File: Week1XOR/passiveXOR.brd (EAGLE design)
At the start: 100 x 80 mm, 27 parts

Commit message: First routing Started
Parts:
- moved JP2 46.2 mm to (49.9, 13.3), turned to 270 degrees
- moved Q5 22.5 mm to (32.0, 8.00), turned to 270 degrees
- moved LED3 19.5 mm to (43.5, 14.1), turned to 180 degrees
- moved R10 16.6 mm to (41.0, 14.1), turned to 90 degrees
- moved LED2 15.5 mm to (23.9, 8.11), turned to 270 degrees
- moved Q10 14.4 mm to (37.0, 20.0), turned to 270 degrees
- moved Q11 13.6 mm to (32.0, 20.0), turned to 270 degrees
- moved R9 13.0 mm to (19.5, 8.11)
- moved LED1 10.1 mm to (24.0, 19.0), turned to 270 degrees
- moved Q2 6.44 mm to (37.0, 8.00), turned to 270 degrees
- moved Q9 5.00 mm to (37.0, 12.0), turned to 270 degrees
- moved R8 4.82 mm to (19.8, 19.0)
- moved Q12 4.00 mm to (32.0, 12.0), turned to 270 degrees
- moved R7 1.53 mm to (15.0, 9.00), turned to 180 degrees
- moved JP1 1.00 mm to (9.16, 12.7)
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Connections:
- removed net COUT: R7.2
- new net OUTC: JP1.4, R7.2
- net A: no longer JP1.2
- net B: no longer JP1.3
- net C: no longer JP1.4
- net INA: now also JP1.2
- net INB: now also JP1.3
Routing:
- net VDD: track 0.00 -> 27.5 mm, vias 0 -> 4
- net NOT1A: track 0.00 -> 7.87 mm
- net NOT2A: track 0.00 -> 7.86 mm
- net NA: track 0.00 -> 7.46 mm
- net NB: track 0.00 -> 7.44 mm
- net NOT2C: track 0.00 -> 6.05 mm
- net NOT1C: track 0.00 -> 6.05 mm
- net N$2: track 0.00 -> 5.38 mm, vias 0 -> 2
- net N$21: track 0.00 -> 5.28 mm, vias 0 -> 2
- net N$3: track 0.00 -> 5.20 mm, vias 0 -> 2
- net B: track 0.00 -> 5.00 mm
- net A: track 0.00 -> 5.00 mm
- net C: track 0.00 -> 3.40 mm
- net N$5: track 0.00 -> 2.59 mm
- net INB: track 0.00 -> 2.00 mm
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
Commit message: More routing and schmatic fixes
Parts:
- moved R1 1.00 mm to (15.0, 18.0)
- moved R2 1.00 mm to (15.0, 16.0)
- moved R3 1.00 mm to (15.0, 14.0)
- moved R4 1.00 mm to (15.0, 12.0)
- moved R7 1.00 mm to (15.0, 10.0)
- moved LED3 0.50 mm to (43.0, 14.0)
- moved JP1 0.34 mm to (9.00, 13.0)
- moved R10 0.10 mm to (41.0, 14.0)
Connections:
- removed net VCC: JP1.1, JP2.1
- net A: no longer JP2.2
- net B: no longer JP2.3
- net C: no longer JP2.4
- net INA: now also JP2.2
- net INB: now also JP2.3
- net OUTC: now also JP2.4
- net VDD: now also JP1.1, JP2.1
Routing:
- net INB: track 2.00 -> 52.5 mm
- net OUTC: track 0.00 -> 45.8 mm
- net C: track 3.40 -> 43.9 mm
- net B: track 5.00 -> 34.2 mm, vias 0 -> 3
- net A: track 5.00 -> 28.1 mm, vias 0 -> 2
- net VDD: track 27.5 -> 36.7 mm, vias 4 -> 5
- net NOT1A: track 7.87 -> 4.00 mm
- net NOT2A: track 7.86 -> 4.00 mm
- net N$4: track 0.00 -> 2.51 mm
- net N$1: track 0.00 -> 2.29 mm

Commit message: More routing Tweaking and started to make pretty
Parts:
- moved JP2 11.4 mm to (39.0, 10.0)
- moved LED1 8.06 mm to (17.0, 15.0)
- moved LED2 8.06 mm to (16.9, 4.11)
- moved LED3 8.06 mm to (36.0, 10.0)
- moved Q1 8.06 mm to (13.0, 12.0)
- moved Q10 8.06 mm to (30.0, 16.0)
- moved Q11 8.06 mm to (25.0, 16.0)
- moved Q12 8.06 mm to (25.0, 8.00)
- moved Q2 8.06 mm to (30.0, 4.00)
- moved Q3 8.06 mm to (30.0, 12.0)
- moved Q4 8.06 mm to (17.0, 12.0)
- moved Q5 8.06 mm to (25.0, 4.00)
- moved Q6 8.06 mm to (25.0, 12.0)
- moved Q7 8.06 mm to (13.0, 8.00)
- moved Q8 8.06 mm to (17.0, 8.00)
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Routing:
- net INB: track 52.5 -> 7.15 mm
- net VDD: track 36.7 -> 77.3 mm
- net N$20: track 0.00 -> 18.5 mm, vias 0 -> 2
- net INA: track 2.00 -> 7.37 mm
- net NOT2A: track 4.00 -> 7.44 mm
- net NOT1A: track 4.00 -> 7.44 mm
- net A: track 28.1 -> 30.2 mm
- net B: track 34.2 -> 35.5 mm
- added copper zone on layer 1, net GND
- added copper zone on layer 16, net GND
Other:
- board size 100 x 80 mm -> 42 x 20 mm
- board text added: "A"
- board text added: "B"
- board text added: "C"
- board text added: "V+"
- board text added: "V-"

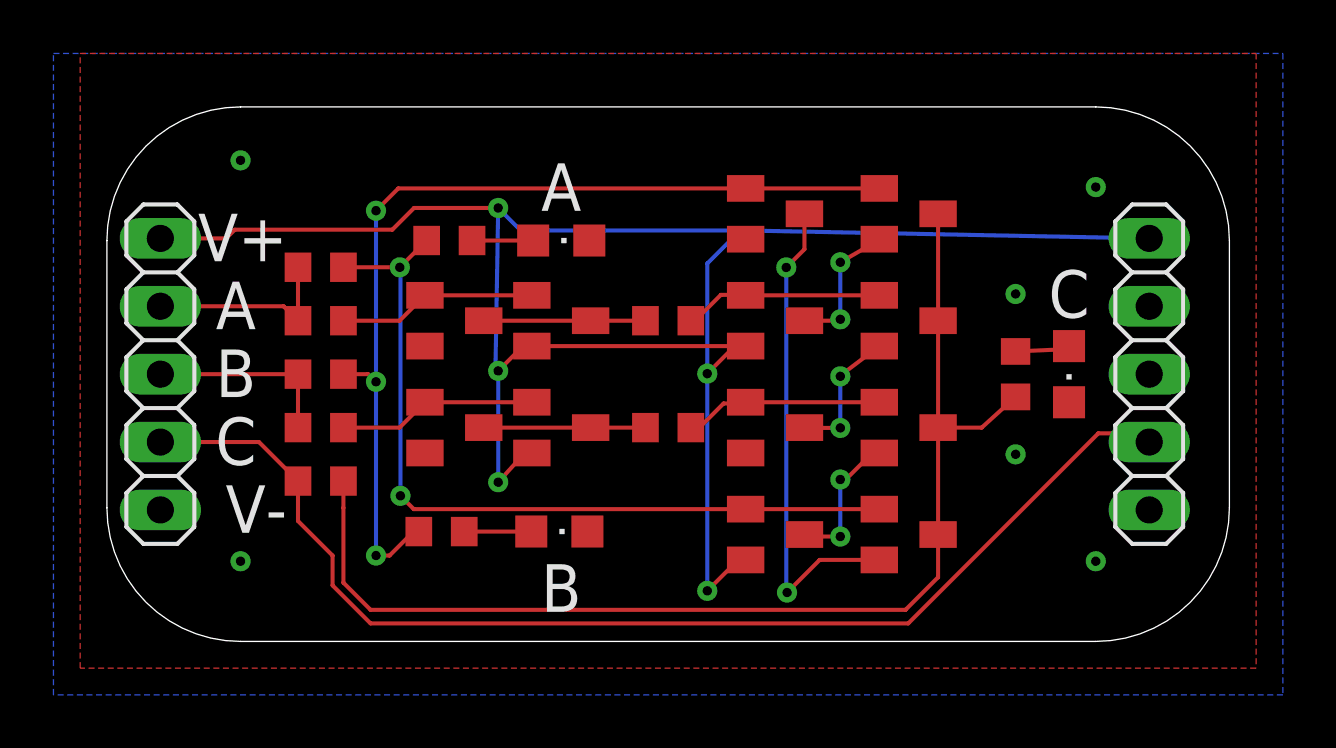
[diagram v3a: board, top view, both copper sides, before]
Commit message: Completed ERC and more desgin tweeks
Completed ERC making sure i have vaules for parts. Changed header through holds to help with distace to the board edge.
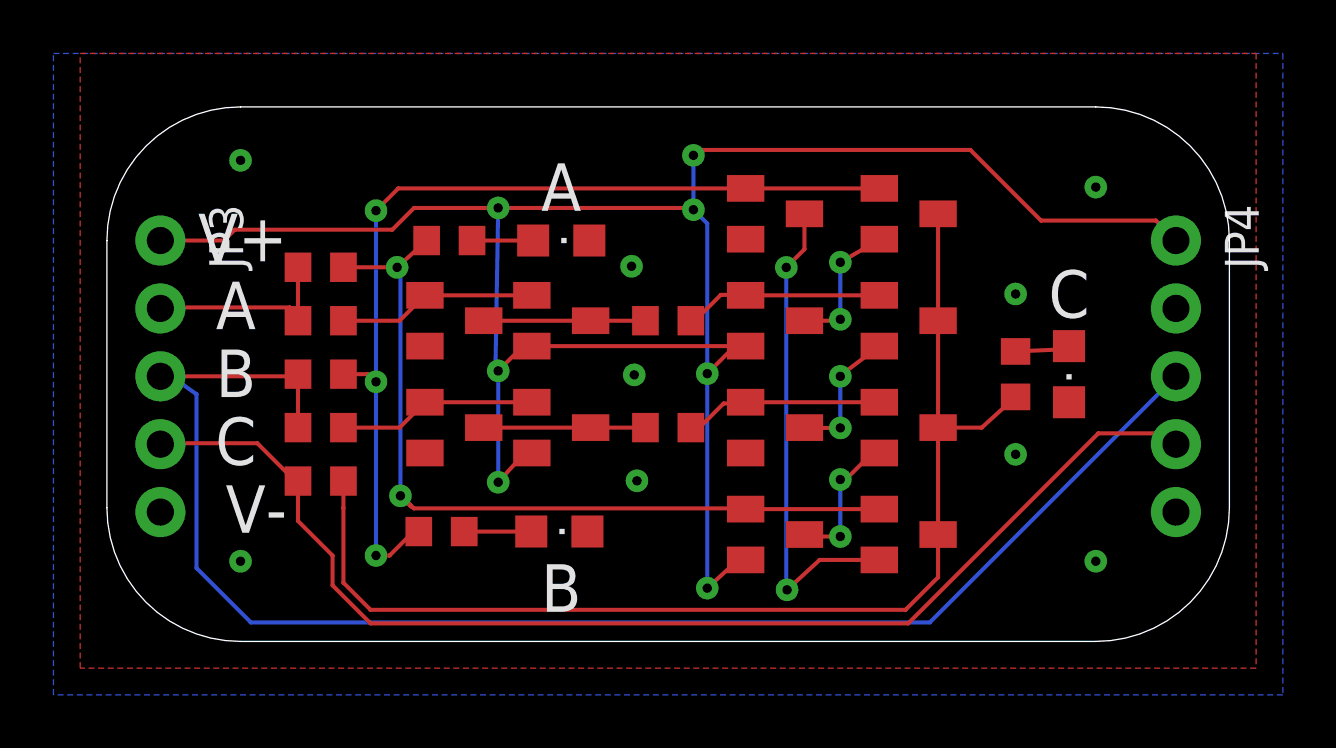
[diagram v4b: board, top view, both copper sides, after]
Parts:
- removed JP1, JP2: (no value), pinhead:1X05
- added JP3, JP4: (no value), SparkFun-Connectors:1X05_NO_SILK
- LED1: value (none) -> Inidcator INA
- LED2: value (none) -> Indicator INB
- LED3: value (none) -> Indicator OUTC
- Q1, Q11, Q2, Q3, Q7: value (none) -> N-Channel
- Q10, Q4, Q5, Q6, Q8, Q9: value (none) -> P-Channel
- Q12: value (none) -> N-channel
- R1, R2, R3, R4, R5, R6, R7: value (none) -> TBD
- R10, R8, R9: value (none) -> 220R
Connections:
- net GND: now also JP3.5, JP4.5; no longer JP1.5, JP2.5
- net INA: now also JP3.2, JP4.2; no longer JP1.2, JP2.2
- net INB: now also JP3.3, JP4.3; no longer JP1.3, JP2.3
- net OUTC: now also JP3.4, JP4.4; no longer JP1.4, JP2.4
- net VDD: now also JP3.1, JP4.1; no longer JP1.1, JP2.1
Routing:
- net INB: track 7.15 -> 56.6 mm
- net VDD: track 77.3 -> 82.1 mm, vias 5 -> 7
- net A: track 30.2 -> 31.4 mm

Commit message: Routing finished
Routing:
- net INA: track 7.29 -> 60.5 mm
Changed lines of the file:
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@@
 <?xml version="1.0" encoding="utf-8"?>
 <!DOCTYPE eagle SYSTEM "eagle.dtd">
-<eagle version="8.4.3">
+<eagle version="8.3.1">
 <drawing>
 <settings>
@@
 <param name="dpMaxLengthDifference" value="0.25mm"/>
 <param name="dpGapFactor" value="2.5"/>
+<param name="checkGrid" value="0"/>
 <param name="checkAngle" value="1"/>
 <param name="checkFont" value="1"/>
 <param name="checkRestrict" value="1"/>
-<param name="checkStop" value="1"/>
 <param name="useDiameter" value="13"/>
 <param name="maxErrors" value="50"/>
@@
 <wire x1="6.8452" y1="12.4968" x2="7.15" y2="12.192" width="0.1524" layer="1"/>
 <wire x1="2.7432" y1="12.4968" x2="6.8452" y2="12.4968" width="0.1524" layer="1"/>
-<wire x1="7.15" y1="12" x2="40" y2="12.46" width="0" layer="19" extent="1-1"/>
+<wire x1="40" y1="12.46" x2="40" y2="11.9584" width="0.1524" layer="16"/>
+<wire x1="40" y1="11.9584" x2="38.4048" y2="10.3632" width="0.1524" layer="16"/>
+<wire x1="38.4048" y1="10.3632" x2="38.4048" y2="8.8392" width="0.1524" layer="16"/>
+<wire x1="30.6832" y1="1.1176" x2="5.4864" y2="1.1176" width="0.1524" layer="16"/>
+<wire x1="5.4864" y1="1.1176" x2="4.6736" y2="1.9304" width="0.1524" layer="16"/>
+<wire x1="4.6736" y1="1.9304" x2="4.663975" y2="1.9304" width="0.1524" layer="16"/>
+<wire x1="4.663975" y1="1.9304" x2="3.7052" y2="2.889175" width="0.1524" layer="16"/>
+<wire x1="3.7052" y1="2.889175" x2="3.7052" y2="9.135690625" width="0.1524" layer="16"/>
+<wire x1="3.7052" y1="9.135690625" x2="3.72454375" y2="9.1628625" width="0.1524" layer="16"/>
+<wire x1="3.72454375" y1="9.1628625" x2="3.7052" y2="9.27779375" width="0.1524" layer="16"/>
+<wire x1="3.7052" y1="9.27779375" x2="3.7052" y2="10.7548" width="0.1524" layer="16"/>
+<wire x1="3.7052" y1="10.7548" x2="2" y2="12.46" width="0.1524" layer="16"/>
+<wire x1="38.4048" y1="8.8392" x2="30.6832" y2="1.1176" width="0.1524" layer="16"/>
 </signal>
 <signal name="INB">

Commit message: Rev1 Finished
DRC finished silk and artwork added documented fonts used
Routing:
- net A: track 31.4 -> 30.6 mm
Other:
- board text removed: "A"
- board text removed: "B"
- board text removed: "C"
- board text removed: "V+"
- board text removed: "V-"
